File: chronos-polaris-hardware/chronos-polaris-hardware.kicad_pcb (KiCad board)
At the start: 2 copper layers, 61 parts, among them J1 Conn_01x03_Pin, J2 Conn_01x03_Pin, J3 Conn_01x03_Pin, J4 Conn_01x03_Pin, J5 Conn_01x03_Pin, J6 Conn_01x04, J7 Conn_01x04, J8 Conn_01x02, P1 WJ124-3_81-6P, U1 TPS62172DSGR, U10 MSK12C02-HB, U12 AP20P30Q, U14 FC-B1010RGBT-HG, U15 TYPE-C_14PLC-H10_0, U2 ESP32-S2-SOLO-2-N4, U3 BMI088, U4 BMP280, U5 TF_PUSH, U6 TLV62130RGTR, U7 AP20P30Q, U8 2N7002KDW_72K

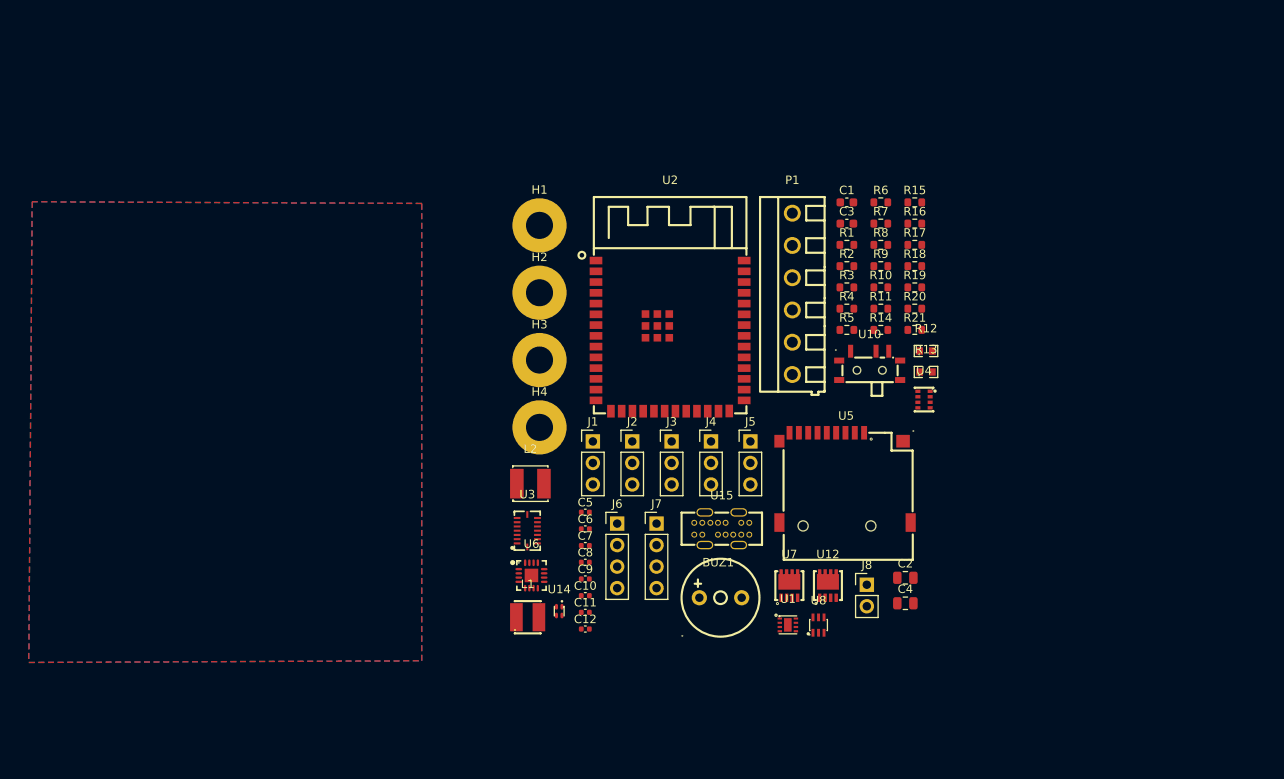
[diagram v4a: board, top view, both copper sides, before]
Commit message: polaris routing with fix V
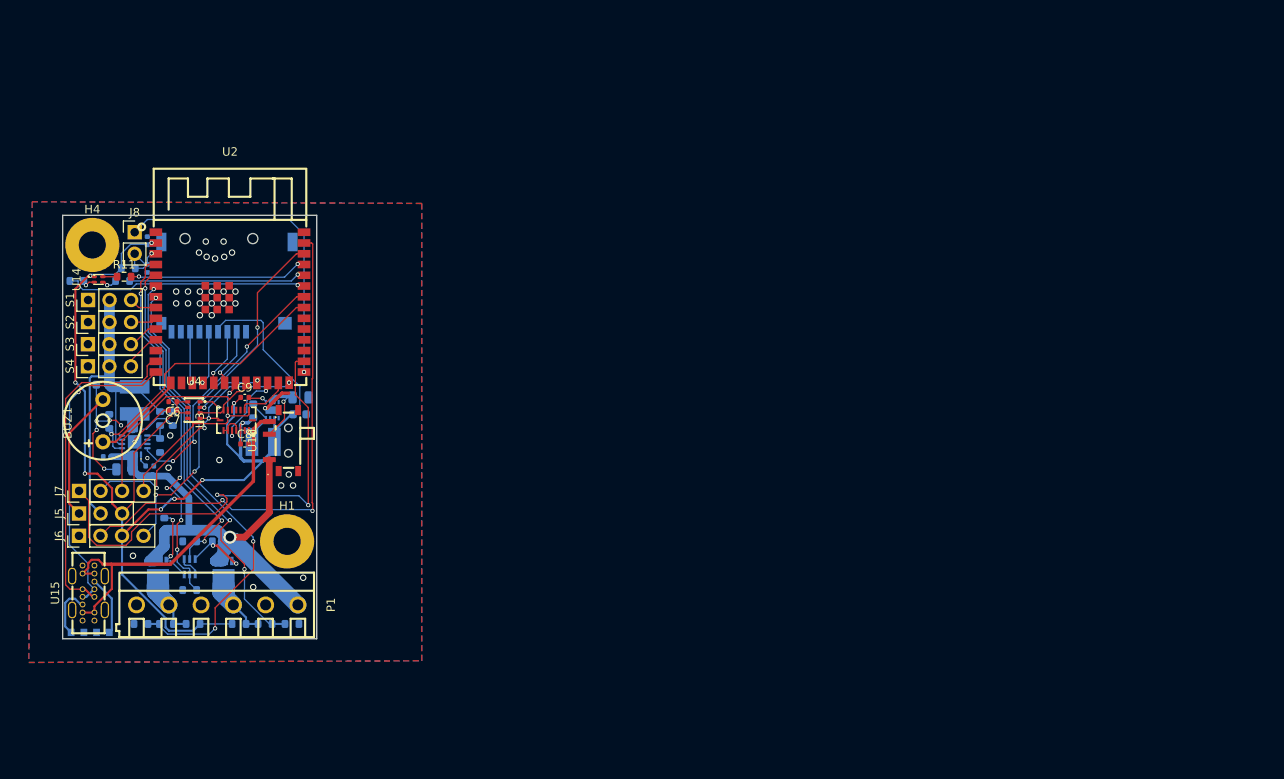
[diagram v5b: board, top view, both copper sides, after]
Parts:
- removed H2, H3: MountingHole, MountingHole:MountingHole_3.2mm_M3_Pad
- C1, C10, C11, C12, C2, C3, C4, C5, L1, L2, R1, R10, R12, R13, R14, R15, R16, R17, R18, R19, R2, R20, R21, R3, R4, R5, R6, R7, R8, R9, U1, U12, U5, U6, U7, U8: moved to B.Cu
- moved R12 105.6 mm to (101.8, 149.2), turned to 180 degrees
- moved R13 101.9 mm to (104.8, 149.2)
- moved R18 100.7 mm to (109.2, 148.2), turned to 180 degrees
- moved R17 99.1 mm to (112.2, 148.2), turned to 180 degrees
- moved R16 97.4 mm to (115.4, 148.2), turned to 180 degrees
- moved J8 96.0 mm to (108.5, 102.0)
- moved R21 95.7 mm to (105.5, 124.3), turned to -90 degrees
- moved R9 94.9 mm to (101.7, 107.8), turned to 180 degrees
- moved C4 93.5 mm to (107.3, 130.0), turned to 180 degrees
- moved R6 90.7 mm to (120.8, 148.2)
- moved R20 90.1 mm to (111.5, 124.0), turned to -90 degrees
- moved C3 89.9 mm to (104.8, 120.0), turned to 180 degrees
- moved R10 89.5 mm to (107.1, 107.8)
- moved R11 89.4 mm to (107.2, 107.2)
- moved R7 89.0 mm to (111.5, 127.2), turned to -90 degrees
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- renumbered J1 to S1, J2 to S2, J3 to S3, J4 to S4
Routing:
- net 3.3V: track 0.00 -> 157.5 mm, vias 0 -> 9
- net /BAT+: track 0.00 -> 69.8 mm, vias 0 -> 1
- net Net-(J6-Pin_2): track 0.00 -> 59.9 mm, vias 0 -> 2
- net Net-(J7-Pin_1): track 0.00 -> 56.9 mm, vias 0 -> 2
- net /DROGUE DETECT: track 0.00 -> 55.1 mm, vias 0 -> 3
- net GND: track 0.00 -> 52.2 mm, vias 0 -> 40
- net /MAIN DETECT: track 0.00 -> 49.0 mm, vias 0 -> 3
- net 5V: track 0.00 -> 46.4 mm
- net /MAIN CTRL: track 0.00 -> 45.0 mm, vias 0 -> 5
- net /USB_5V: track 0.00 -> 43.2 mm
- net Net-(J6-Pin_4): track 0.00 -> 42.7 mm, vias 0 -> 3
- net /DROGUE CTRL: track 0.00 -> 40.2 mm, vias 0 -> 3
- net Net-(U2-IO19): track 0.00 -> 39.2 mm
- net /GPIO0 (BOOTLOADER): track 0.00 -> 37.6 mm, vias 0 -> 1
- net Net-(U2-IO20): track 0.00 -> 36.8 mm, vias 0 -> 1
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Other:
- board outline added: 30 x 50 mm

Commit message: minor fixes
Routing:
- net /BAT+: track 69.8 -> 68.8 mm
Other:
- outline, holes or cut-outs redrawn
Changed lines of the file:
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@@
     (property "ki_keywords" "R res resistor")
     (attr smd)
-    (fp_text reference "R11" (at 0 -1.43) (layer "F.SilkS")
+    (fp_text reference "R11" (at 0.446 -1.43) (layer "F.SilkS")
         (effects (font (size 1 1) (thickness 0.15)))
     )
@@
     )
   )
-  (gr_rect (start 100 100) (end 130 150)
-    (stroke (width 0.1) (type default)) (fill none) (layer "Edge.Cuts"))
+  (gr_arc (start 130 149) (mid 129.707107 149.707107) (end 129 150)
+    (stroke (width 0.1) (type default)) (layer "Edge.Cuts"))
+  (gr_line (start 100 149) (end 100 101)
+    (stroke (width 0.1) (type default)) (layer "Edge.Cuts"))
+  (gr_arc (start 100 101) (mid 100.292893 100.292893) (end 101 100)
+    (stroke (width 0.1) (type default)) (layer "Edge.Cuts"))
+  (gr_line (start 101 100) (end 129 100)
+    (stroke (width 0.1) (type default)) (layer "Edge.Cuts"))
+  (gr_arc (start 101 150) (mid 100.292893 149.707107) (end 100 149)
+    (stroke (width 0.1) (type default)) (layer "Edge.Cuts"))
+  (gr_arc (start 129 100) (mid 129.707107 100.292893) (end 130 101)
+    (stroke (width 0.1) (type default)) (layer "Edge.Cuts"))
+  (gr_line (start 130 101) (end 130 149)
+    (stroke (width 0.1) (type default)) (layer "Edge.Cuts"))
+  (gr_line (start 129 150) (end 101 150)
+    (stroke (width 0.1) (type default)) (layer "Edge.Cuts"))
   (segment (start 119.497968 124.902032) (end 119.497968 125.399796) (width 0.15) (layer "F.Cu") (net 1))
   (segment (start 120.497968 124.824917) (end 120.273051 124.6) (width 0.15) (layer "F.Cu") (net 1))
@@
   (segment (start 105.525 117.841842) (end 105.520178 117.83702) (width 1.27) (layer "B.Cu") (net 5))
   (segment (start 103.2 133.93094) (end 103.2 119.222592) (width 0.25) (layer "B.Cu") (net 5))
-  (segment (start 124.399924 135.100076) (end 121.5 138) (width 0.8) (layer "F.Cu") (net 6))
-  (segment (start 124.399924 128.849885) (end 124.399924 135.100076) (width 0.8) (layer "F.Cu") (net 6))
-  (segment (start 121.5 138) (end 119.75 138) (width 0.8) (layer "F.Cu") (net 6))
+  (segment (start 119.81 138) (end 119.75 138) (width 0.8) (layer "F.Cu") (net 6))
+  (segment (start 124.399924 133.410076) (end 119.81 138) (width 0.8) (layer "F.Cu") (net 6))
+  (segment (start 124.399924 128.849885) (end 124.399924 133.410076) (width 0.8) (layer "F.Cu") (net 6))
   (via (at 119.75 138) (size 1.524) (drill 1.016) (layers "F.Cu" "B.Cu") (net 6))
   (segment (start 119.325 138.5) (end 118.937479 138.887521) (width 1.27) (layer "B.Cu") (net 6))

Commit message: silkscreen
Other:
- board text added: "+"
- board text added: "-"
- board text added: "3v3"
- board text added: "5-20V"
- board text added: "5v"
- board text added: "C1"
- board text added: "C2"
- board text added: "CHRONOS ROCKETRY"
- board text added: "GND"
- board text added: "POLARIS"
- board text added: "REV 1 FC"
- board text added: "S"
- board text added: "VIN"

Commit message: random qol updates?
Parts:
- added R22: 30k, Resistor_SMD:R_0603_1608Metric, B.Cu at (125.8, 117.2)
- added R23: 10k, Resistor_SMD:R_0603_1608Metric, B.Cu at (125.8, 115.4)
- renumbered S1 to J1, S2 to J2, S3 to J3, S4 to J4
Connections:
- net Net-(U1-EN) renamed VIN
- U2 pad 29: unconnected-(U2-IO36-Pad29) -> VIN_1/4
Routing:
- net VIN_1/4: track 0.00 -> 4.43 mm, vias 0 -> 1
- net VIN: track 9.65 -> 14.0 mm, vias 1 -> 2
- net 3.3V: track 157.5 -> 153.2 mm, vias 9 -> 11
- net Net-(J4-Pin_3): track 4.64 -> 3.48 mm
- net Net-(U1-SW): track 4.22 -> 3.21 mm
- net /MISO / SDO: track 25.2 -> 24.2 mm
- net /MAIN DETECT: track 49.0 -> 48.3 mm
- net /DROGUE V+: track 9.67 -> 8.90 mm
- net Net-(U2-IO19): track 39.2 -> 38.5 mm
- net Net-(U2-IO12): track 7.08 -> 6.41 mm
- net Net-(J7-Pin_1): track 56.9 -> 57.5 mm
- net /MOSI / SDI: track 28.5 -> 27.9 mm
- net GND: track 52.2 -> 52.7 mm, vias 40 -> 46
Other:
- board text added: "3.5-13V"
- board text added: "CS SPICLK SDI SDO"
- board text added: "G/5/3V3"
- board text added: "G/IO1/3V3/IO2"
- board text removed: "5-20V"
